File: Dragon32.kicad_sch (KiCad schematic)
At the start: 7 parts, among them IC14 74LS86, IC22 74LS00, IC23 74LS74, IC25 LM393, IC28 74LS393, IC31 74LS02

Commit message: update drawings
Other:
- company: (none) -> Dragon Data
- title: (none) -> Dragon 32 CPU UK Issue 2
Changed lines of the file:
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@@
 (kicad_sch (version 20211123) (generator eeschema)
   (paper "A3")
+  (title_block
+    (title "Dragon 32 CPU UK Issue 2")
+    (date "2022-09-25")
+    (rev "1")
+    (company "Dragon Data")
+    (comment 1 "Reproduced and Modified by Julian Brown")
+  )
   (junction (at 371.729 121.539) (diameter 0) (color 0 0 0 0)
   )

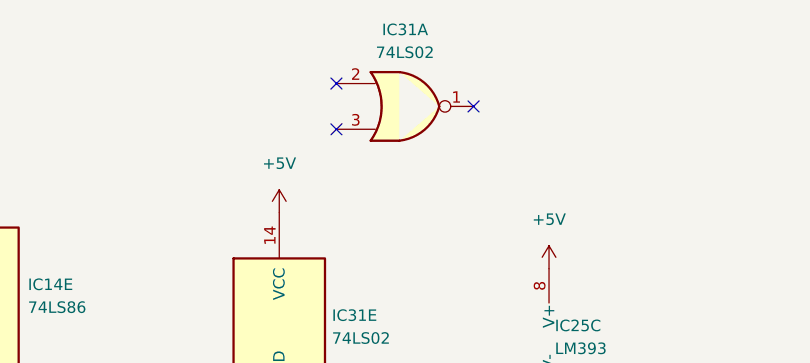
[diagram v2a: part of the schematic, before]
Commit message: add 64k switch
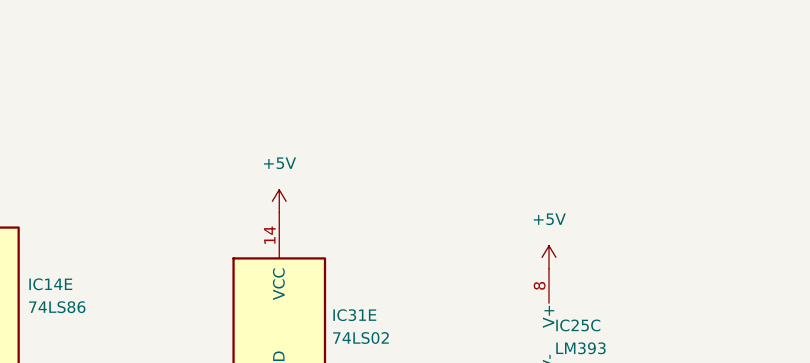
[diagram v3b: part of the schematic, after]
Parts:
- removed unit 1 of IC31
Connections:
- no-connect marks 3 -> 0
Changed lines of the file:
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@@
   (junction (at 371.729 37.719) (diameter 0) (color 0 0 0 0)
   )
-  (no_connect (at 87.503 25.4))
-  (no_connect (at 72.263 22.86))
-  (no_connect (at 72.263 27.94))
   (wire (pts (xy 371.729 118.999) (xy 371.729 121.539))
     (stroke (width 0) (type default) (color 0 0 0 0))
@@
       (effects (font (size 1.27 1.27)) hide)
     )
-    (pin "1")
-    (pin "2")
-    (pin "3")
-    (pin "5")
-    (pin "6")
-    (pin "7")
     (pin "4")
     (pin "8")
@@
       (effects (font (size 1.27 1.27)) hide)
     )
-    (pin "1")
-    (pin "2")
-    (pin "3")
-    (pin "4")
-    (pin "5")
-    (pin "6")
-    (pin "10")
-    (pin "11")
-    (pin "12")
-    (pin "13")
-    (pin "8")
-    (pin "9")
     (pin "14")
     (pin "7")
   )
-  (symbol (lib_id "74xx:74LS02") (at 79.883 25.4 0) (unit 1)
-    (in_bom yes) (on_board yes) (fields_autoplaced)
-    (property "Reference" "IC31" (id 0) (at 79.883 16.891 0))
-    (property "Value" "74LS02" (id 1) (at 79.883 19.431 0))
-    (property "Footprint" "Package_DIP:DIP-14_W7.62mm" (id 2) (at 79.883 25.4 0)
-      (effects (font (size 1.27 1.27)) hide)
-    )
-    (property "Datasheet" "http://www.ti.com/lit/gpn/sn74ls02" (id 3) (at 79.883 25.4 0)
+  (symbol (lib_id "power:GND") (at 67.056 110.617 0) (unit 1)
+    (in_bom yes) (on_board yes) (fields_autoplaced)
+    (property "Reference" "#PWR0113" (id 0) (at 67.056 116.967 0)
+      (effects (font (size 1.27 1.27)) hide)
+    )
+    (property "Value" "GND" (id 1) (at 67.056 115.316 0))
+    (property "Footprint" "" (id 2) (at 67.056 110.617 0)
+      (effects (font (size 1.27 1.27)) hide)
+    )
+    (property "Datasheet" "" (id 3) (at 67.056 110.617 0)
       (effects (font (size 1.27 1.27)) hide)
     )
     (pin "1")
-    (pin "2")
-    (pin "3")
-    (pin "4")
-    (pin "5")
-    (pin "6")
-    (pin "10")
-    (pin "8")
-    (pin "9")
-    (pin "11")
-    (pin "12")
-    (pin "13")
+  )
+  (symbol (lib_id "74xx:74LS00") (at 68.072 144.145 0) (unit 5)
+    (in_bom yes) (on_board yes) (fields_autoplaced)
+    (property "Reference" "IC22" (id 0) (at 74.93 142.8749 0)
+      (effects (font (size 1.27 1.27)) (justify left))
+    )
+    (property "Value" "74LS00" (id 1) (at 74.93 145.4149 0)
+      (effects (font (size 1.27 1.27)) (justify left))
+    )
+    (property "Footprint" "Package_DIP:DIP-14_W7.62mm" (id 2) (at 68.072 144.145 0)
+      (effects (font (size 1.27 1.27)) hide)
+    )
+    (property "Datasheet" "http://www.ti.com/lit/gpn/sn74ls00" (id 3) (at 68.072 144.145 0)
+      (effects (font (size 1.27 1.27)) hide)
+    )
     (pin "14")
     (pin "7")
   )
-  (symbol (lib_id "power:GND") (at 67.056 110.617 0) (unit 1)
-    (in_bom yes) (on_board yes) (fields_autoplaced)
-    (property "Reference" "#PWR0113" (id 0) (at 67.056 116.967 0)
-      (effects (font (size 1.27 1.27)) hide)
-    )
-    (property "Value" "GND" (id 1) (at 67.056 115.316 0))
-    (property "Footprint" "" (id 2) (at 67.056 110.617 0)
-      (effects (font (size 1.27 1.27)) hide)
-    )
-    (property "Datasheet" "" (id 3) (at 67.056 110.617 0)
+  (symbol (lib_id "power:+5V") (at 31.877 33.782 0) (unit 1)
+    (in_bom yes) (on_board yes) (fields_autoplaced)
+    (property "Reference" "#PWR0109" (id 0) (at 31.877 37.592 0)
+      (effects (font (size 1.27 1.27)) hide)
+    )
+    (property "Value" "+5V" (id 1) (at 31.877 28.321 0))
+    (property "Footprint" "" (id 2) (at 31.877 33.782 0)
+      (effects (font (size 1.27 1.27)) hide)
+    )
+    (property "Datasheet" "" (id 3) (at 31.877 33.782 0)
       (effects (font (size 1.27 1.27)) hide)
     )
     (pin "1")
   )
-  (symbol (lib_id "74xx:74LS00") (at 68.072 144.145 0) (unit 5)
-    (in_bom yes) (on_board yes) (fields_autoplaced)
-    (property "Reference" "IC22" (id 0) (at 74.93 142.8749 0)
+  (symbol (lib_id "power:GND") (at 370.84 121.539 270) (unit 1)
+    (in_bom yes) (on_board yes) (fields_autoplaced)
+    (property "Reference" "#PWR0102" (id 0) (at 364.49 121.539 0)
+      (effects (font (size 1.27 1.27)) hide)
+    )
+    (property "Value" "GND" (id 1) (at 367.538 121.5389 90)
+      (effects (font (size 1.27 1.27)) (justify right))
+    )
+    (property "Footprint" "" (id 2) (at 370.84 121.539 0)
+      (effects (font (size 1.27 1.27)) hide)
+    )
+    (property "Datasheet" "" (id 3) (at 370.84 121.539 0)
+      (effects (font (size 1.27 1.27)) hide)
+    )
+    (pin "1")
+  )
+  (symbol (lib_id "74xx:74LS74") (at 33.655 96.139 0) (unit 3)
+    (in_bom yes) (on_board yes) (fields_autoplaced)
+    (property "Reference" "IC23" (id 0) (at 40.64 94.8689 0)
       (effects (font (size 1.27 1.27)) (justify left))
     )
-    (property "Value" "74LS00" (id 1) (at 74.93 145.4149 0)
+    (property "Value" "74LS74" (id 1) (at 40.64 97.4089 0)
       (effects (font (size 1.27 1.27)) (justify left))
     )
-    (property "Footprint" "Package_DIP:DIP-14_W7.62mm" (id 2) (at 68.072 144.145 0)
-      (effects (font (size 1.27 1.27)) hide)
-    )
-    (property "Datasheet" "http://www.ti.com/lit/gpn/sn74ls00" (id 3) (at 68.072 144.145 0)
-      (effects (font (size 1.27 1.27)) hide)
-    )
-    (pin "1")
-    (pin "2")
-    (pin "3")
-    (pin "4")
-    (pin "5")
-    (pin "6")
-    (pin "10")
-    (pin "8")
-    (pin "9")
-    (pin "11")
-    (pin "12")
-    (pin "13")
+    (property "Footprint" "Package_DIP:DIP-14_W7.62mm" (id 2) (at 33.655 96.139 0)
+      (effects (font (size 1.27 1.27)) hide)
+    )
+    (property "Datasheet" "74xx/74hc_hct74.pdf" (id 3) (at 33.655 96.139 0)
+      (effects (font (size 1.27 1.27)) hide)
+    )
     (pin "14")
     (pin "7")
   )
-  (symbol (lib_id "power:+5V") (at 31.877 33.782 0) (unit 1)
-    (in_bom yes) (on_board yes) (fields_autoplaced)
-    (property "Reference" "#PWR0109" (id 0) (at 31.877 37.592 0)
-      (effects (font (size 1.27 1.27)) hide)
-    )
-    (property "Value" "+5V" (id 1) (at 31.877 28.321 0))
-    (property "Footprint" "" (id 2) (at 31.877 33.782 0)
-      (effects (font (size 1.27 1.27)) hide)
-    )
-    (property "Datasheet" "" (id 3) (at 31.877 33.782 0)
-      (effects (font (size 1.27 1.27)) hide)
-    )
-    (pin "1")
-  )
-  (symbol (lib_id "power:GND") (at 370.84 121.539 270) (unit 1)
-    (in_bom yes) (on_board yes) (fields_autoplaced)
-    (property "Reference" "#PWR0102" (id 0) (at 364.49 121.539 0)
-      (effects (font (size 1.27 1.27)) hide)
-    )
-    (property "Value" "GND" (id 1) (at 367.538 121.5389 90)
-      (effects (font (size 1.27 1.27)) (justify right))
-    )
-    (property "Footprint" "" (id 2) (at 370.84 121.539 0)
-      (effects (font (size 1.27 1.27)) hide)
-    )
-    (property "Datasheet" "" (id 3) (at 370.84 121.539 0)
-      (effects (font (size 1.27 1.27)) hide)
-    )
-    (pin "1")
-  )
-  (symbol (lib_id "74xx:74LS74") (at 33.655 96.139 0) (unit 3)
-    (in_bom yes) (on_board yes) (fields_autoplaced)
-    (property "Reference" "IC23" (id 0) (at 40.64 94.8689 0)
-      (effects (font (size 1.27 1.27)) (justify left))
-    )
-    (property "Value" "74LS74" (id 1) (at 40.64 97.4089 0)
-      (effects (font (size 1.27 1.27)) (justify left))
-    )
-    (property "Footprint" "Package_DIP:DIP-14_W7.62mm" (id 2) (at 33.655 96.139 0)
-      (effects (font (size 1.27 1.27)) hide)
-    )
-    (property "Datasheet" "74xx/74hc_hct74.pdf" (id 3) (at 33.655 96.139 0)
-      (effects (font (size 1.27 1.27)) hide)
-    )
-    (pin "1")
-    (pin "2")
-    (pin "3")
-    (pin "4")
-    (pin "5")
-    (pin "6")
-    (pin "10")
-    (pin "11")
-    (pin "12")
-    (pin "13")
-    (pin "8")
-    (pin "9")
-    (pin "14")
-    (pin "7")
-  )
   (symbol (lib_id "power:GND") (at 95.885 58.674 0) (unit 1)
     (in_bom yes) (on_board yes) (fields_autoplaced)
@@
       (effects (font (size 1.27 1.27)) hide)
     )
-    (pin "1")
-    (pin "2")
-    (pin "3")
-    (pin "4")
-    (pin "5")
-    (pin "6")
-    (pin "10")
-    (pin "8")
-    (pin "9")
-    (pin "11")
-    (pin "12")
-    (pin "13")
     (pin "14")
     (pin "7")
@@
       (effects (font (size 1.27 1.27)) hide)
     )
-    (pin "1")
-    (pin "2")
-    (pin "3")
-    (pin "4")
-    (pin "5")
-    (pin "6")
-    (pin "10")
-    (pin "8")
-    (pin "9")
-    (pin "11")
-    (pin "12")
-    (pin "13")
     (pin "14")
     (pin "7")
@@
       (reference "#PWR0156") (unit 1) (value "GND") (footprint "")
     )
-    (path "/c0eaba02-6b8d-4a7f-b51d-5746c573781a/8829f984-f966-4976-8d6b-d6d7d498c5d7"
-      (reference "#PWR0157") (unit 1) (value "GND") (footprint "")
-    )
     (path "/c0eaba02-6b8d-4a7f-b51d-5746c573781a/bcc89797-aacc-42b8-a5df-8aa7d601176a"
       (reference "#PWR0158") (unit 1) (value "+5V") (footprint "")
@@
       (reference "#PWR0277") (unit 1) (value "GND") (footprint "")
     )
+    (path "/c0eaba02-6b8d-4a7f-b51d-5746c573781a/d40e7a14-7c72-4079-89d9-7b21d77ccf2d"
+      (reference "#PWR?") (unit 1) (value "GND") (footprint "")
+    )
     (path "/64d8d7b7-14ab-4042-9ee8-f1aec24a139c/4818ed6d-32a2-406d-951d-2e9a9511d8c8"
       (reference "C1") (unit 1) (value "0.1uF") (footprint "Capacitor_THT:C_Disc_D3.0mm_W2.0mm_P2.50mm")
@@
       (reference "IC30") (unit 5) (value "74LS32") (footprint "Package_DIP:DIP-14_W7.62mm")
     )
-    (path "/35befaeb-a0e8-4f8f-be3b-9bdc67a1d19c"
+    (path "/c0eaba02-6b8d-4a7f-b51d-5746c573781a/874d9926-d0ca-4759-922c-3bfaa7161447"
       (reference "IC31") (unit 1) (value "74LS02") (footprint "Package_DIP:DIP-14_W7.62mm")
     )
@@
       (reference "JP11-12") (unit 1) (value "printer/comms") (footprint "Connector_PinHeader_2.54mm:PinHeader_1x03_P2.54mm_Vertical")
     )
+    (path "/c0eaba02-6b8d-4a7f-b51d-5746c573781a/118a4ba8-2d1e-4b84-b32b-428f469598f2"
+      (reference "JP13-14") (unit 1) (value "16k/32k") (footprint "Connector_PinHeader_2.54mm:PinHeader_1x03_P2.54mm_Vertical")
+    )
     (path "/64d8d7b7-14ab-4042-9ee8-f1aec24a139c/f5bf5a18-fba1-47cc-bd81-826923cdc9aa"
